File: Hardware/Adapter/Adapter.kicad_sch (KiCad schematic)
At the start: 4 parts

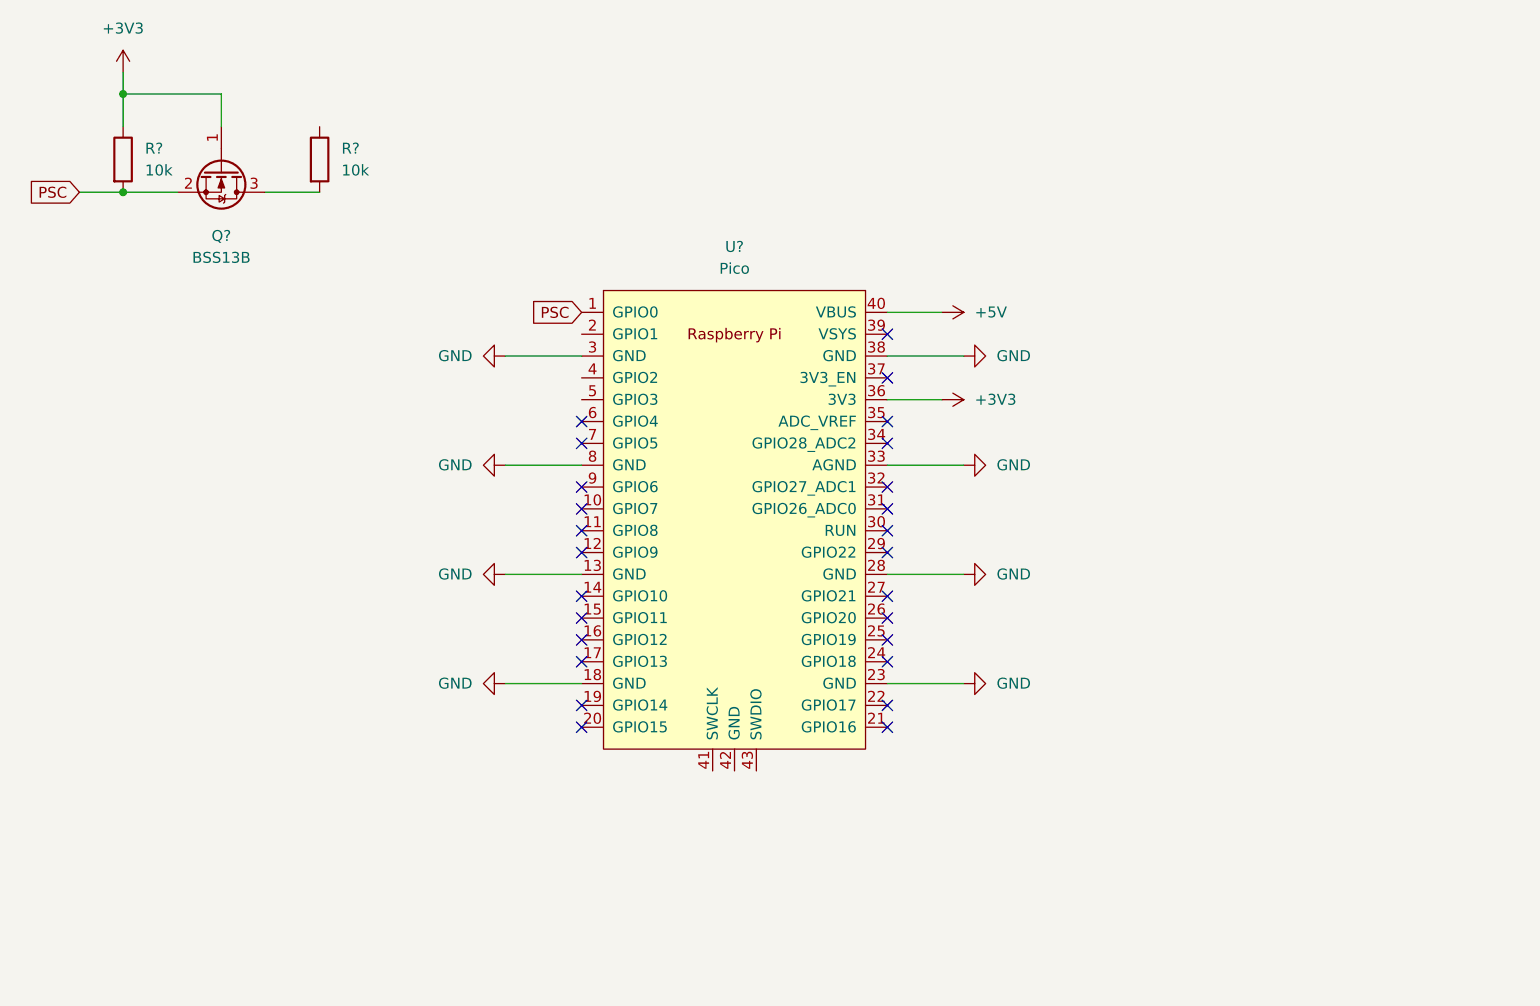
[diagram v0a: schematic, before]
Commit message: Work on adapter and changed some camera settings
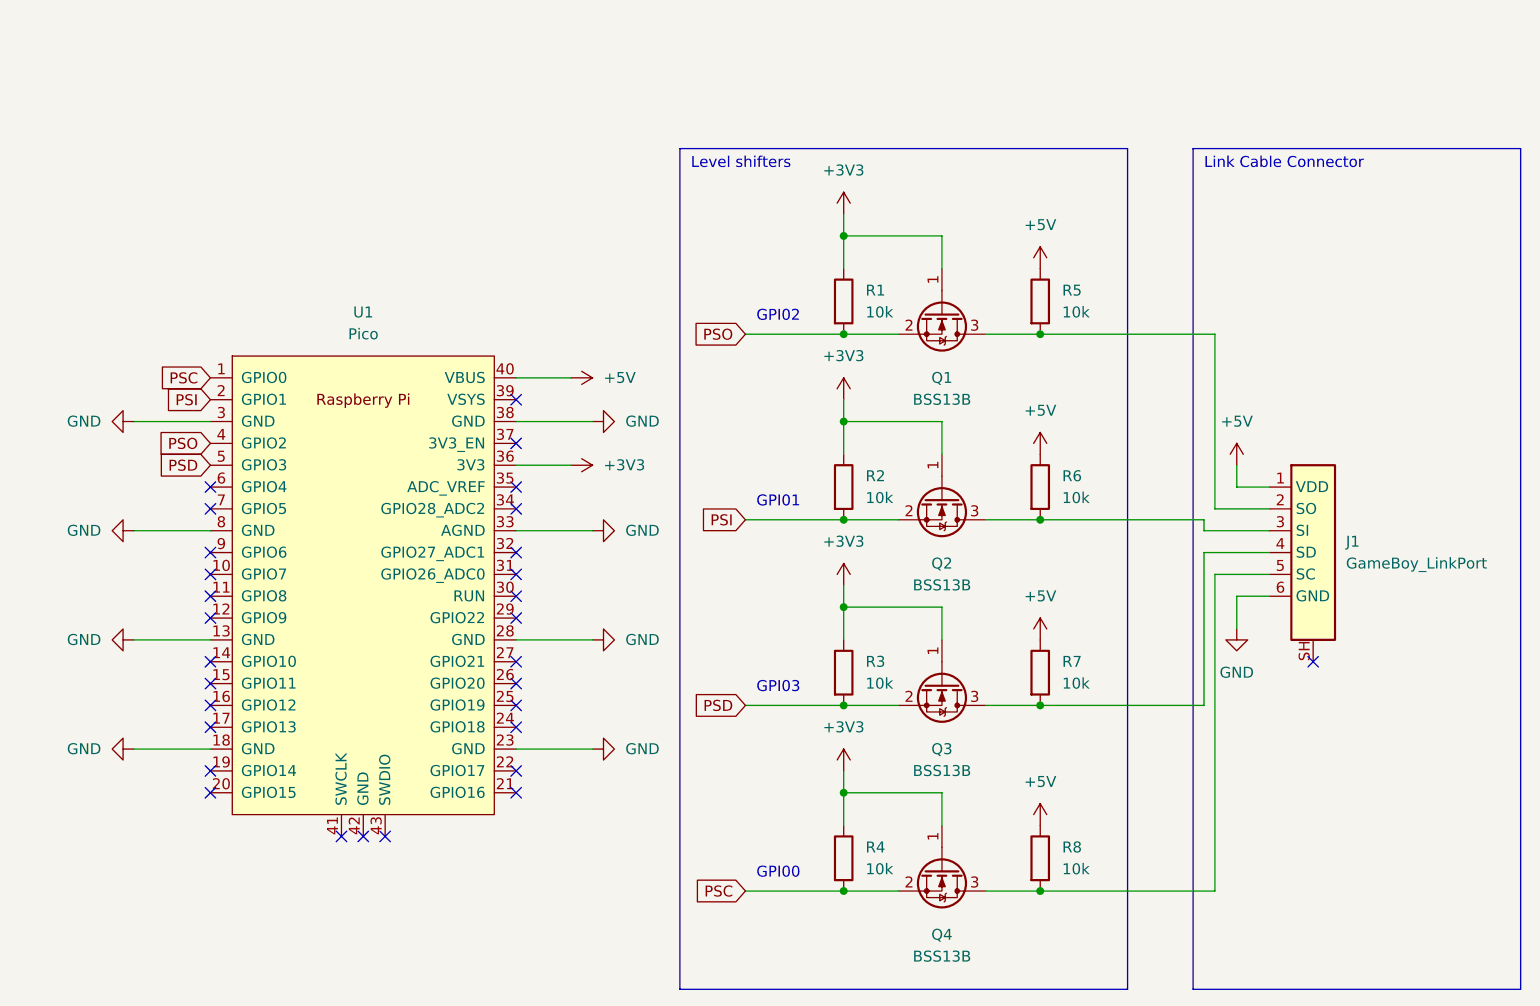
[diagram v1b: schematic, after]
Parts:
- added J1: GameBoy_LinkPort, Gekkio_Connector:GameBoy_LinkPort_MGB_Horizontal, symbol gameboy_linkport:GameBoy_LinkPort
- added Q2, Q3, Q4: BSS13B, Package_TO_SOT_SMD:SOT-23, symbol Device:Q_NMOS_GSD
- added R2, R3, R4, R6, R7, R8: 10k, Resistor_SMD:R_0402_1005Metric, symbol Device:R
- Q1: renamed from Q?; footprint (none) -> Package_TO_SOT_SMD:SOT-23
- R1, R5: renamed from R?; footprint (none) -> Resistor_SMD:R_0402_1005Metric
- gave numbers to parts that had none: 1
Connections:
- net +3V3: now also Q2.1 (G), Q3.1 (G), Q4.1 (G), R2.1, R3.1, R4.1
- net +5V: now also R5.1, J1.1 (VDD), R6.1, R7.1, R8.1
- net GND: now also J1.6 (GND)
- net PSC: now also Q4.2 (S), R4.2; no longer Q1.2 (S), R1.2
- net PSI: now reaches U1.2 (GPIO1)
- net PSI: now also Q2.2 (S), R2.2
- net PSO: now reaches U1.4 (GPIO2)
- net PSO: now also Q1.2 (S), R1.2
- net PSD: now reaches U1.5 (GPIO3)
- net PSD: now also Q3.2 (S), R3.2
- net at Q1.3 (D), R5.2: now also J1.2 (SO)
- new net: J1.5 (SC), Q4.3 (D), R8.2
- new net: J1.3 (SI), Q2.3 (D), R6.2
- new net: J1.4 (SD), Q3.3 (D), R7.2
- no-connect marks 26 -> 30
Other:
- note added: "GPI00"
- note added: "GPI01"
- note added: "GPI02"
- note added: "GPI03"
- note added: "Level shifters"
- note added: "Link Cable Connector"
- company: (none) -> Squaresweets Games
- title: (none) -> TileWorld GBA Adapter
- moved on the sheet: Q1, R1, R5, U1
